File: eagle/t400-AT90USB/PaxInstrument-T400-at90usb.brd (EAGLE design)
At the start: 99.1 x 53.3 mm, 138 parts, among them IC1 MCP3424, IC2 AT90USB1287-AU, IC3 SN74LVC1G74DCT, J1 MICRO-SDCARD-CONNECTOR-330006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, Q1 DMP2035U-7, Q2 DMP2035U-7, Q3 DMN2075U-7, Q4 DMN2075U-7, Q5 DMP2035U-7, U1 MCP9800, U2 APX809, U3 MCP73831, U4 MIC5219-3.3V, X1 FH12-12S-1S, Y1 RESONATORSMD

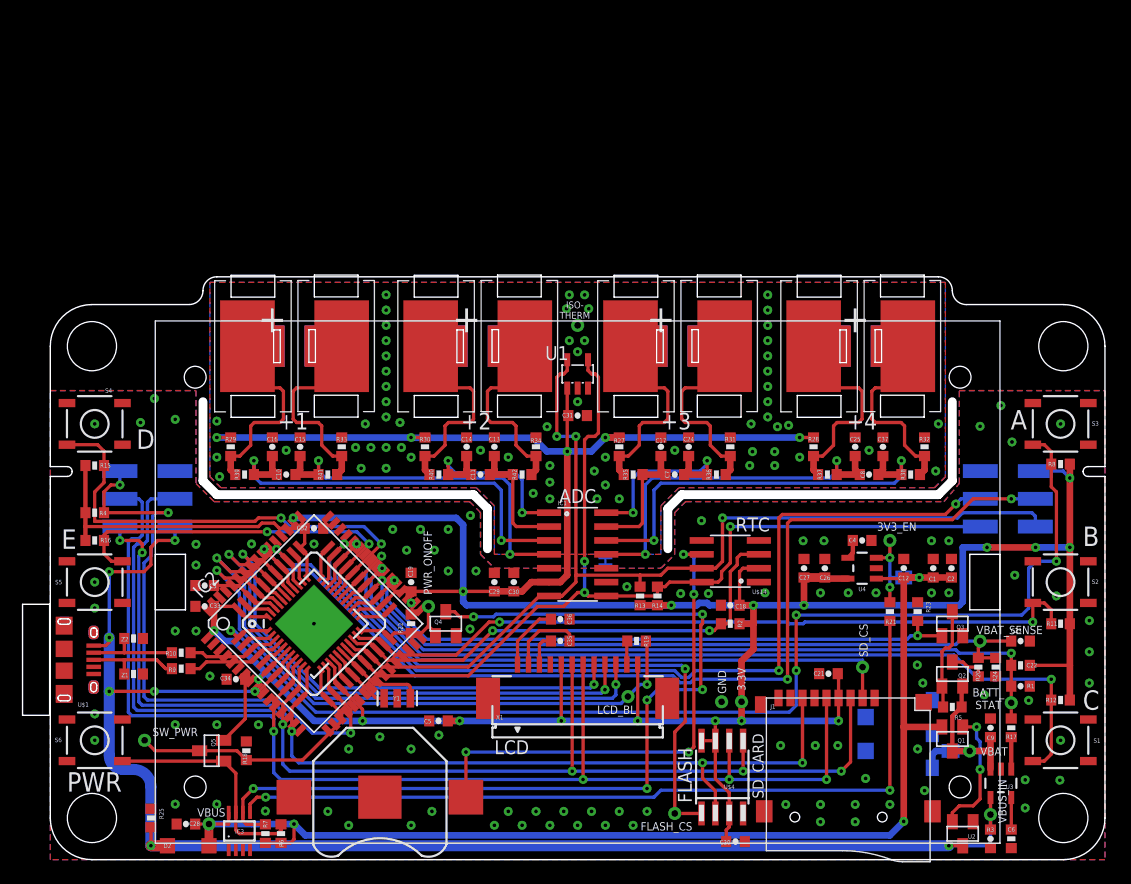
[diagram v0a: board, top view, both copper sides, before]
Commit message: Added T400 location PDF. Moved component names on PCB file.
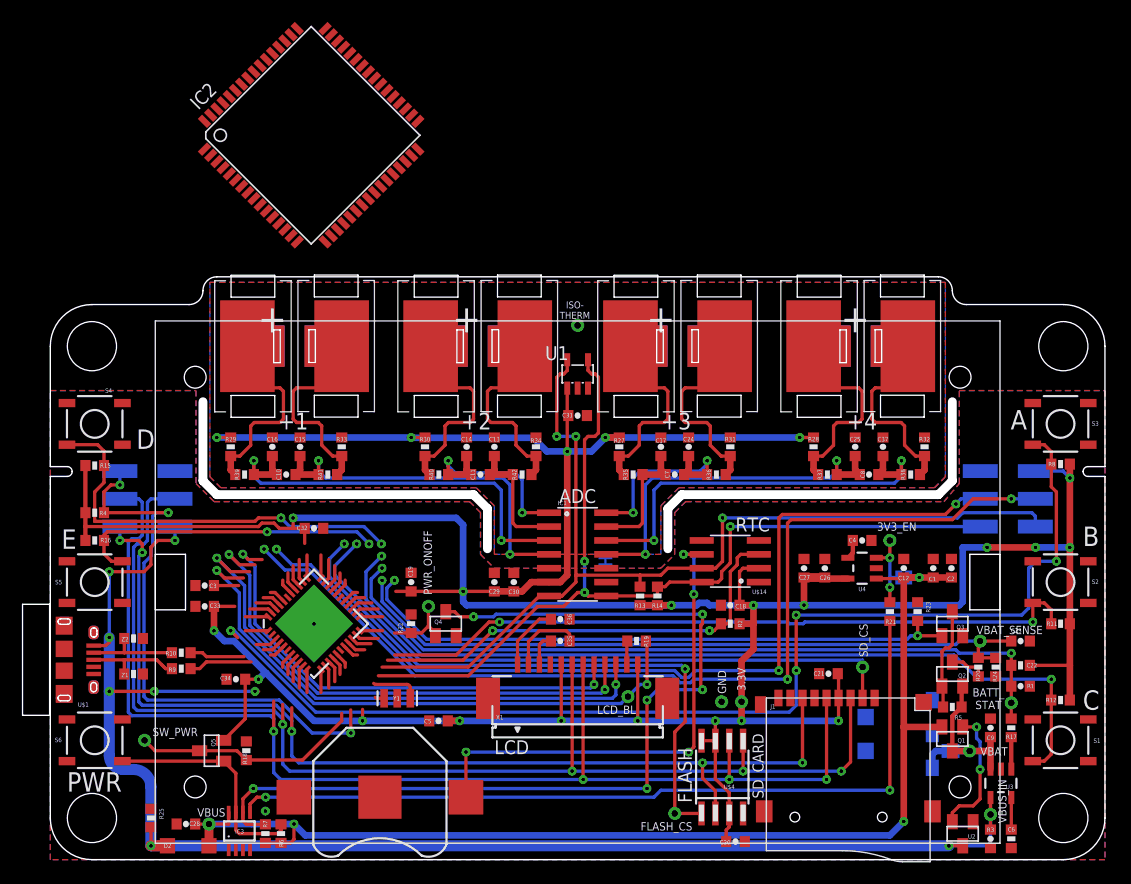
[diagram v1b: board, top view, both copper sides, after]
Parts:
- removed U$3: SPARKFUN-DIGITALIC_ATMEGA32U4TQFP, PaxInstrument-T400:SPARKFUN-DIGITALIC_SPARKFUN-DIGITALIC_TQFP44
- moved IC2 44.7 mm to (23.9, 66.3)
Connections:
- removed net N$17: GND.2, U$3.2
- net 3.3V: no longer U$3.14, U$3.24, U$3.34, U$3.44, U$3.6
- net AREF: no longer U$3.42
- net BATT_STAT: no longer U$3.27
- net D+: no longer U$3.4
- net D-: no longer U$3.3
- net DATA1: no longer U$3.37
- net DATA2: no longer U$3.36
- net FLASH_CS: no longer U$3.32
- net GND: no longer U$3.15, U$3.23, U$3.33, U$3.35, U$3.43, U$3.5
- net LCD_A0: no longer U$3.38
- net LCD_BL: no longer U$3.41
- net LCD_CS: no longer U$3.40
- net LCD_RST: no longer U$3.39
- net MISO: no longer U$3.11
- net MOSI: no longer U$3.10
- net PWR_ONOFF: no longer U$3.22
- net RESET: no longer U$3.13
- net RTC_INT: no longer U$3.20
- net RXLED: no longer U$3.8
- net SCK: no longer U$3.9
- net SCL: no longer U$3.18
- net SDA: no longer U$3.19
- net SD_CS: no longer U$3.31
- net SW_A: no longer U$3.1
- net SW_B: no longer U$3.21
- net SW_C: no longer U$3.28
- net SW_D: no longer U$3.29
- net SW_E: no longer U$3.30
- net SW_PWR: no longer U$3.12
- net VBAT_EN: no longer U$3.25
- net VBAT_SENSE: no longer U$3.26
- net VBUS_IN: no longer U$3.7
- net XTAL1: no longer U$3.17
- net XTAL2: no longer U$3.16
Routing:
- net 3.3V: track 387.4 -> 374.9 mm
- net SW_C: track 84.5 -> 79.1 mm
- net GND: track 17.0 -> 12.0 mm, vias 94 -> 1
- net SW_D: track 44.0 -> 39.3 mm
- net XTAL1: track 8.79 -> 4.46 mm
- net LCD_RST: track 51.8 -> 47.6 mm
- net XTAL2: track 6.28 -> 2.40 mm
- net SW_E: track 34.1 -> 30.3 mm
- net BATT_STAT: track 74.5 -> 71.4 mm
- net VBUS_IN: track 143.9 -> 140.7 mm
- net DATA1: track 95.9 -> 92.8 mm
- net VBAT_EN: track 60.8 -> 57.9 mm
- net N$17: track 2.90 -> 0.00 mm
- net RESET: track 56.6 -> 53.8 mm
- net SD_CS: track 63.6 -> 60.7 mm
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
